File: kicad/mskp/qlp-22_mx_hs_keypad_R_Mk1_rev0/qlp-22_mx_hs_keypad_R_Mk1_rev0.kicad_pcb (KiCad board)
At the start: 2 copper layers, 175.4 x 84.9 mm, 28 parts, among them J1 Conn_01x12_Socket, SW1 Switch, SW10 Switch, SW11 Switch, SW2 Switch, SW3 Switch, SW4 Switch, SW5 Switch, SW6 Switch, SW7 Switch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

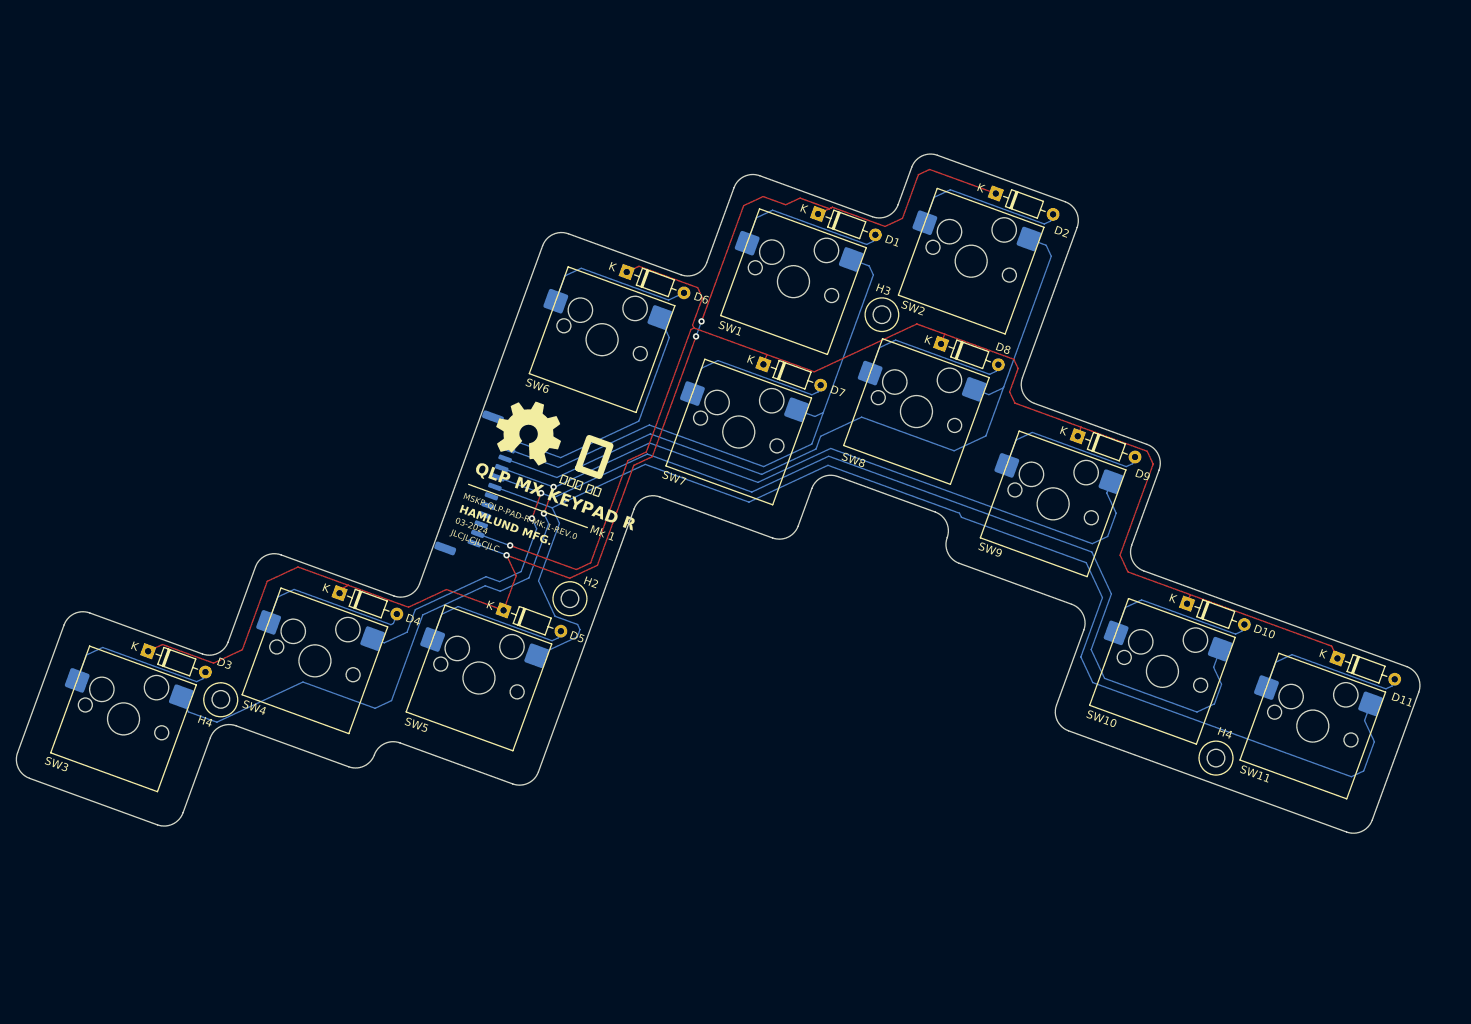
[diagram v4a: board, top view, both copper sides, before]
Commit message: Adds right side case to mskp qlp test case
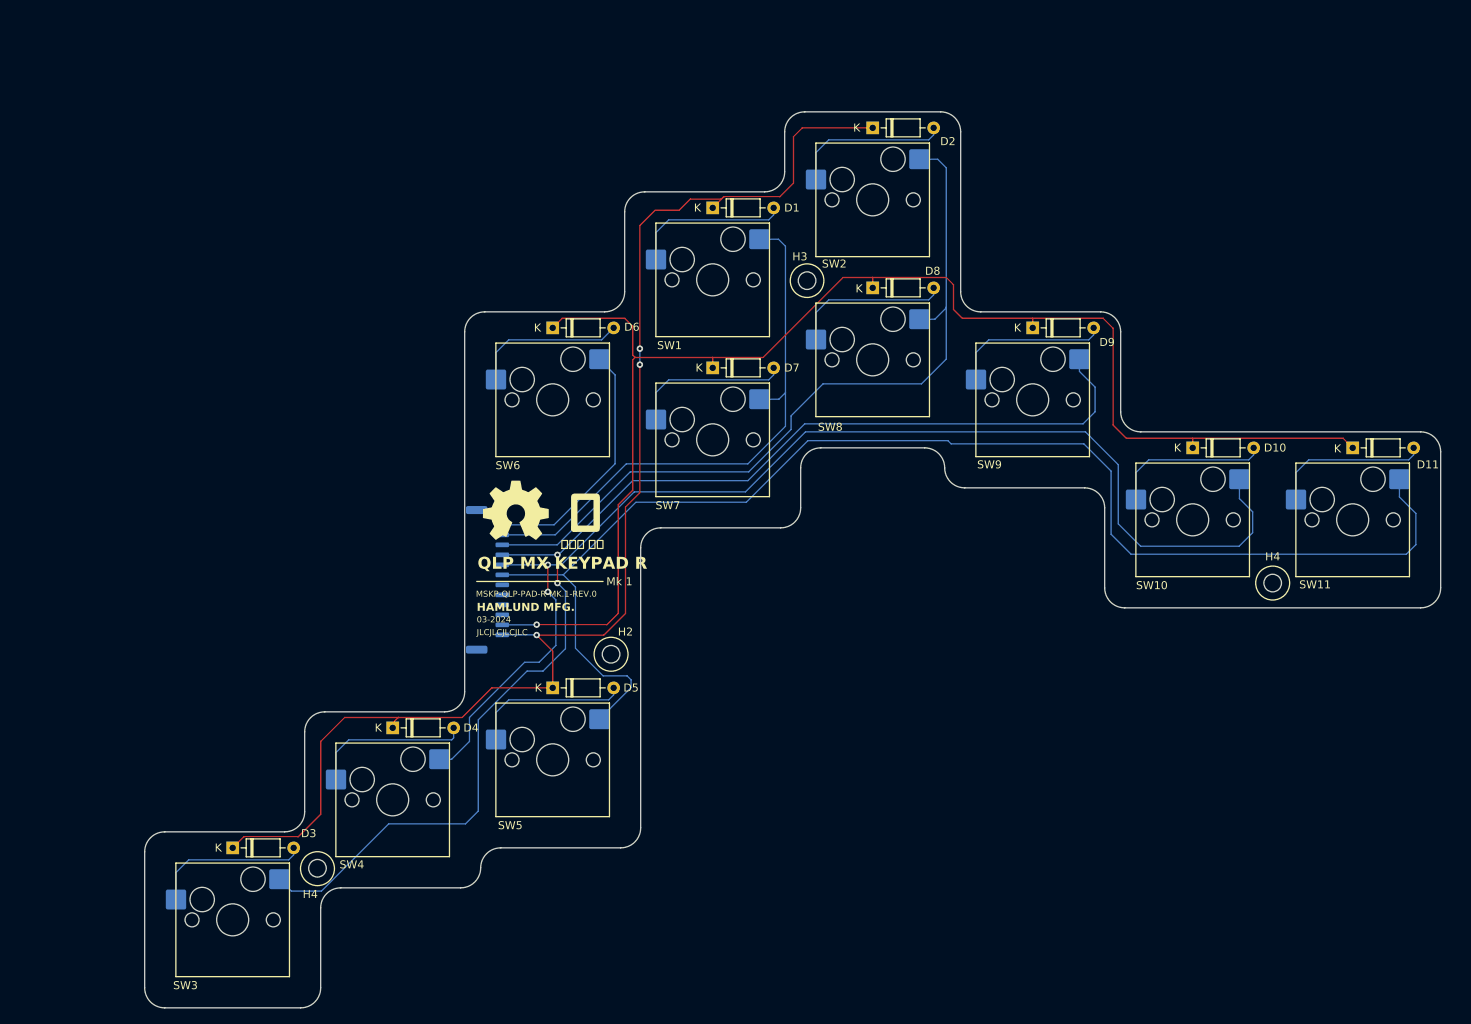
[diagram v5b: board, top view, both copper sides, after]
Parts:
- moved SW3 28.6 mm to (87.7, 147.3), turned to 0 degrees
- moved D3 26.8 mm to (87.7, 138.3), turned to 0 degrees
- moved D11 26.4 mm to (227.7, 88.3), turned to 0 degrees
- moved SW11 26.3 mm to (227.7, 97.3), turned to 0 degrees
- moved H4 24.3 mm to (98.3, 140.9), turned to 0 degrees
- moved H4 23.0 mm to (217.7, 105.2), turned to 0 degrees
- moved SW4 19.9 mm to (107.7, 132.3), turned to 0 degrees
- moved D10 19.5 mm to (207.7, 88.3), turned to 0 degrees
- moved SW10 19.3 mm to (207.7, 97.3), turned to 0 degrees
- moved D4 18.1 mm to (107.7, 123.3), turned to 0 degrees
- moved D2 17.4 mm to (167.7, 48.3), turned to 0 degrees
- moved D9 14.7 mm to (187.7, 73.3), turned to 0 degrees
- moved SW2 14.5 mm to (167.7, 57.3), turned to 0 degrees
- moved SW5 13.8 mm to (127.7, 127.3), turned to 0 degrees
- moved SW9 13.2 mm to (187.7, 82.3), turned to 0 degrees
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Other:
- board size 175.4 x 84.9 mm -> 162 x 112 mm
